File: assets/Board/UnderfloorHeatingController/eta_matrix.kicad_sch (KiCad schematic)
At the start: 0 parts

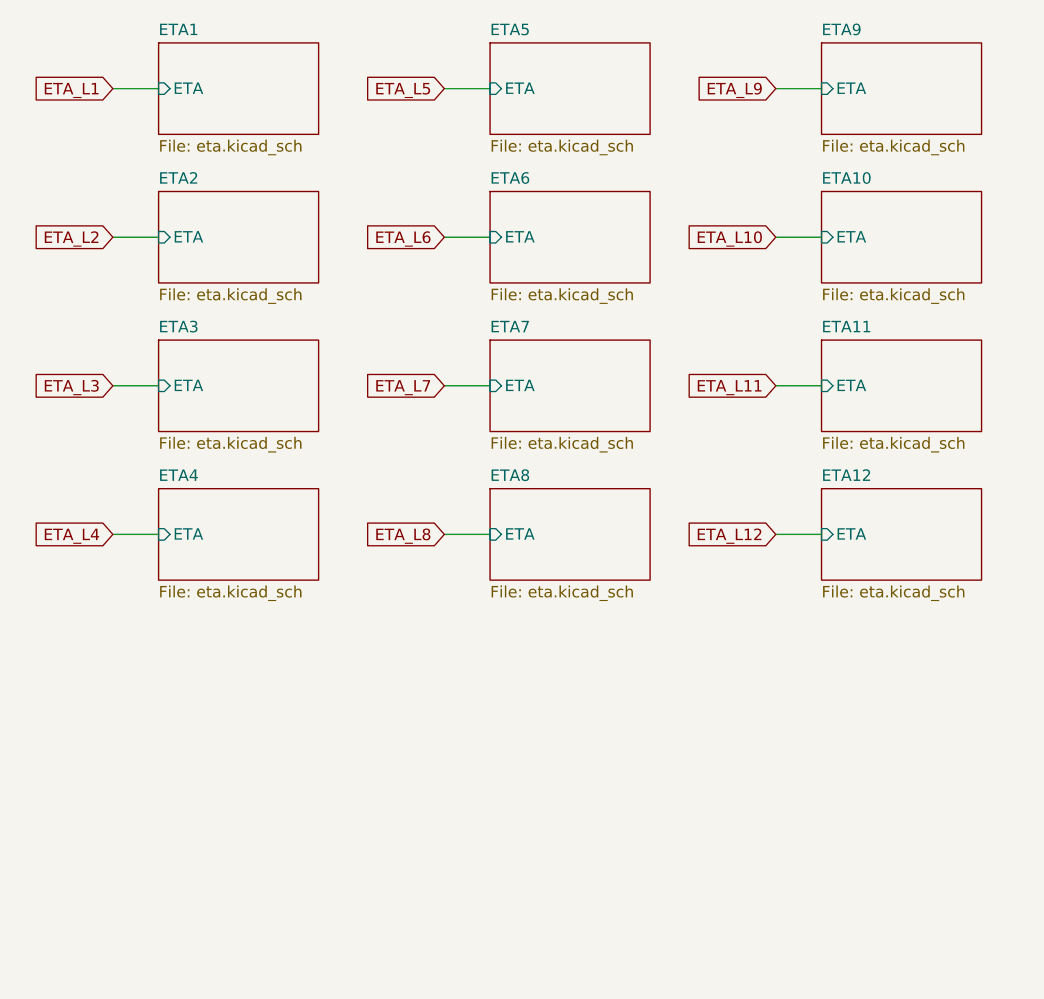
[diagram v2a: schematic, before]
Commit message: First version of the redesigned controller.
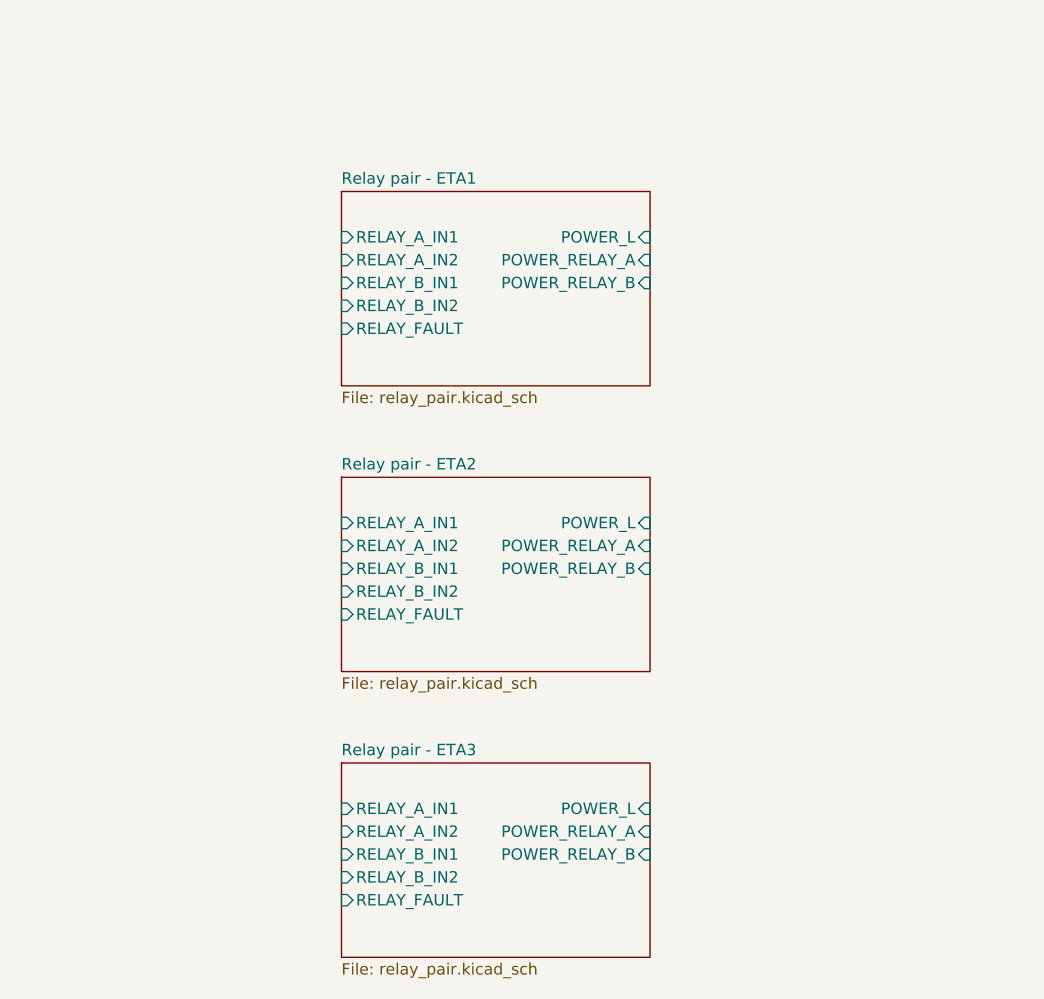
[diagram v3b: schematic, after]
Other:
- removed sheet ETA1
- removed sheet ETA10
- removed sheet ETA11
- removed sheet ETA12
- removed sheet ETA2
- removed sheet ETA3
- removed sheet ETA4
- removed sheet ETA5
- removed sheet ETA6
- removed sheet ETA7
- removed sheet ETA8
- removed sheet ETA9
- added sheet Relay pair - ETA1 (relay_pair.kicad_sch)
- added sheet Relay pair - ETA2 (relay_pair.kicad_sch)
- added sheet Relay pair - ETA3 (relay_pair.kicad_sch)
